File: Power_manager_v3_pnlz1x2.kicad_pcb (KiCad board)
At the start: 4 copper layers, 50 x 50 mm, 160 parts, among them J1 L_input, J2 Pow_mng_pow, J3 Load1, J4 Load2, J5 SWD (PLS5), J6 Dig_mod_iface, Q1 2N5551S, Q2 2N5551S, U1 DC12003, U2 G3MB-202PL, U3 G3MB-202PL, U4 DC5V_DC5V3V3_v3, U5 STM32F030F4Px, U6 HLW8112, U7 ADuM_I2C_v3, Y1 CSTCE8M, Y2 ABLS-3.579545MHZ-D-3-Y-T

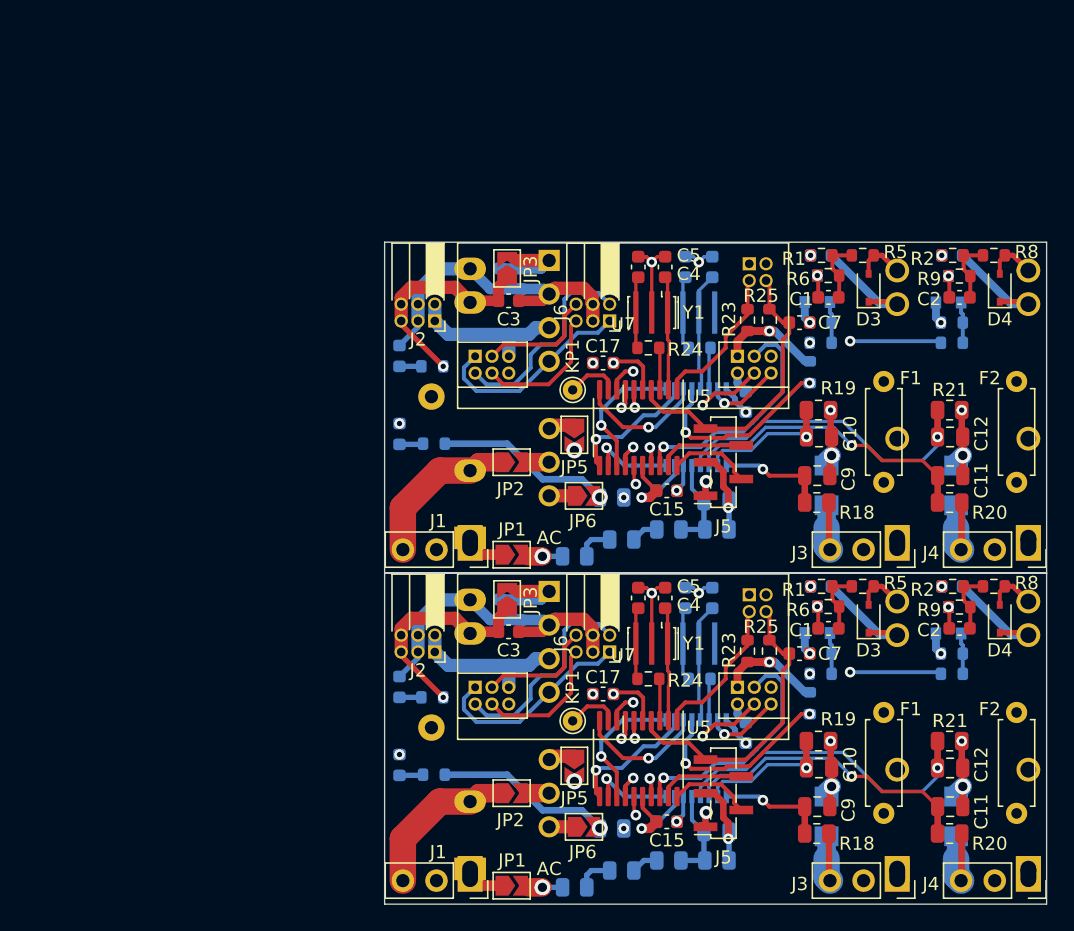
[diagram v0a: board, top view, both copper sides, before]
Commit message: Сформирован перечень элементов, 3D-модель, исправлены ошибки, реализована панелизация платы.
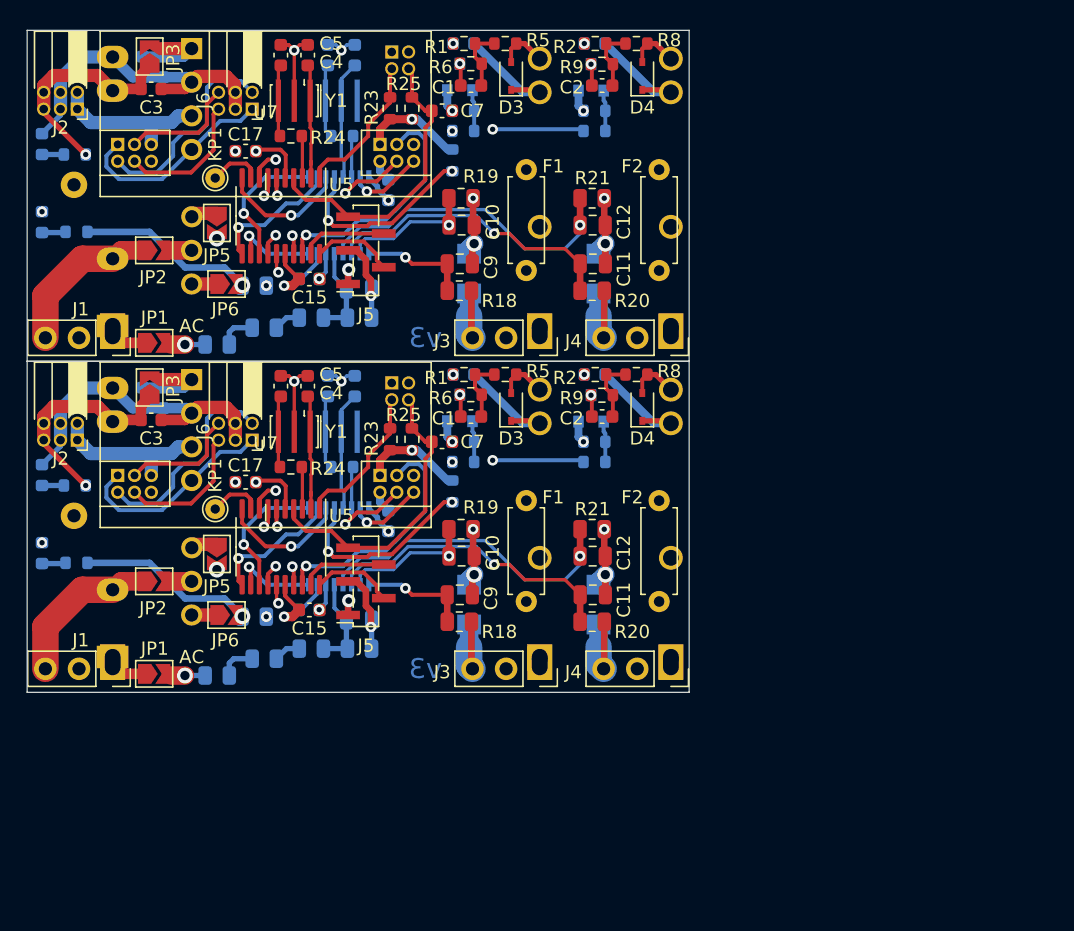
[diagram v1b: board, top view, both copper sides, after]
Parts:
- moved J4 31.4 mm to (108.6, 99.2)
- moved J4 31.4 mm to (108.6, 74.2)
- moved Q2 31.4 mm to (102.6, 79.6)
- moved Q2 31.4 mm to (102.6, 54.6)
- moved U3 31.4 mm to (108.6, 98.5)
- moved U3 31.4 mm to (108.6, 73.5)
- moved GND1 31.4 mm to (63.5, 87.7)
- moved GND1 31.4 mm to (63.5, 62.7)
- moved C18 31.4 mm to (84.7, 52.9)
- moved C19 31.4 mm to (82.7, 52.9)
- moved C4 31.4 mm to (81.2, 52.9)
- moved C5 31.4 mm to (79.2, 52.9)
- moved JP4 31.4 mm to (87.5, 52.6)
- moved U7 31.4 mm to (78.0, 63.6)
- moved C1 31.4 mm to (93.5, 80.2)
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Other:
- board text added: "v3"
